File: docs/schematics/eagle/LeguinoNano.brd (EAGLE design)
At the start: 111.4 x 73.7 mm, 32 parts, among them Q1 60V/32A/35m?, Q2 60V/32A/35m?, Q3 60V/32A/35m?, Q4 60V/32A/35m?, Q5 60V/32A/35m?

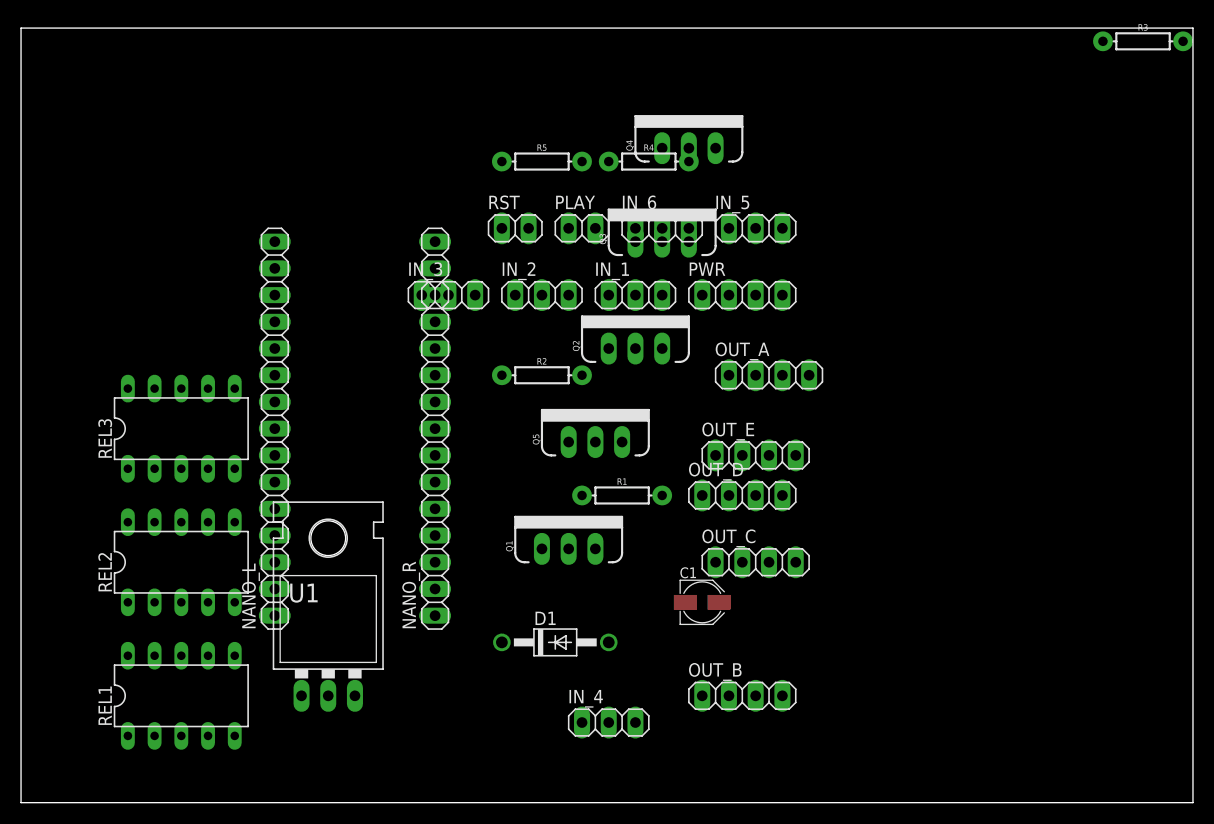
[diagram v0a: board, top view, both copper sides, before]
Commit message: Continued EAGLE schematic and board for Arduino Uno.
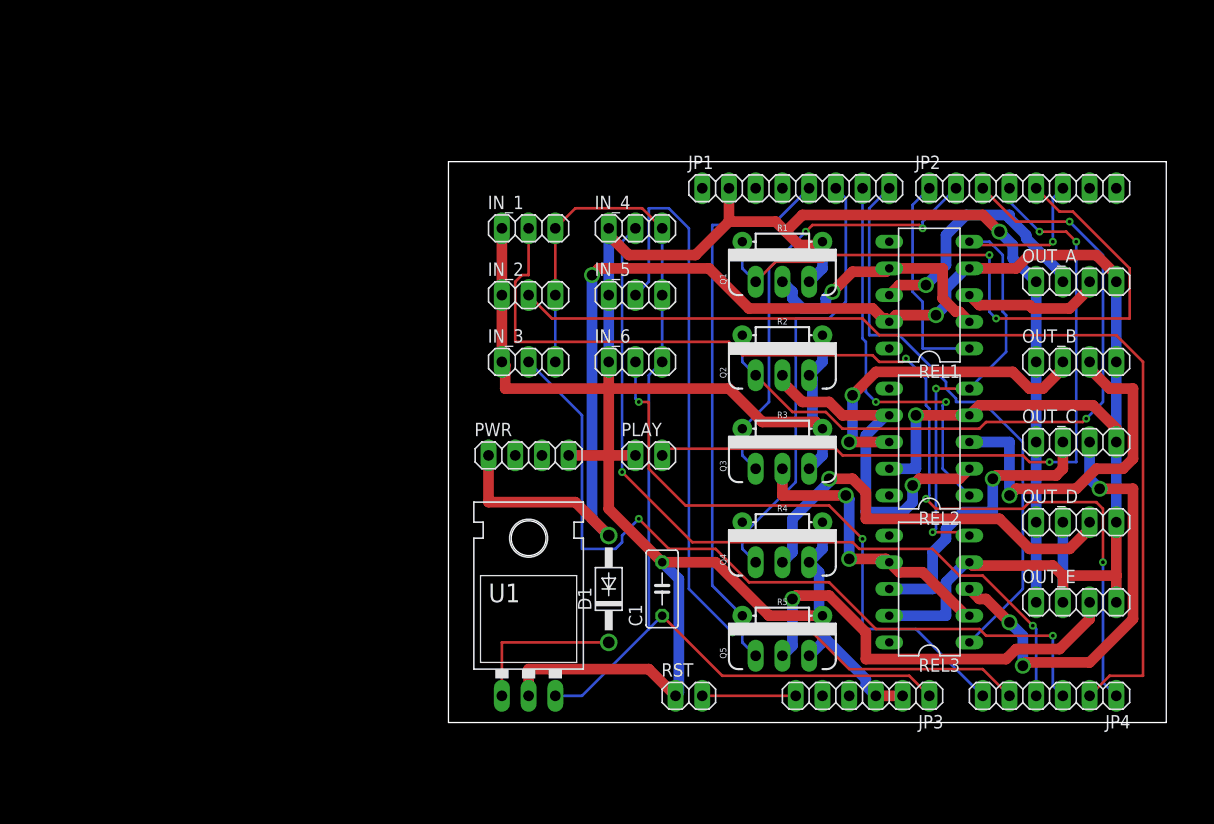
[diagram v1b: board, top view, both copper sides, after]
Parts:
- removed NANO_L, NANO_R: (no value), pinhead:1X15
- added JP1, JP2: (no value), pinhead:1X08
- added JP3, JP4: (no value), pinhead:1X06
- C1: device resistor:PANASONIC_B -> adafruit:C050-030X075
- moved REL1 80.7 mm to (86.4, 48.3), turned to 90 degrees
- moved REL3 72.7 mm to (86.4, 20.3), turned to 90 degrees
- moved REL2 72.0 mm to (86.4, 34.3), turned to 90 degrees
- moved R3 50.3 mm to (72.4, 35.6)
- moved R5 48.9 mm to (72.4, 17.8)
- moved RST 47.4 mm to (63.5, 10.2)
- moved IN_4 47.1 mm to (58.4, 54.6)
- moved OUT_B 44.9 mm to (100.3, 41.9)
- moved Q4 40.4 mm to (72.4, 22.9)
- moved R4 36.6 mm to (72.4, 26.7)
- moved OUT_E 33.5 mm to (100.3, 19.1)
- moved OUT_C 32.6 mm to (100.3, 34.3)
- moved Q1 32.5 mm to (72.4, 49.5)
- moved OUT_D 31.9 mm to (100.3, 26.7)
- moved OUT_A 30.5 mm to (100.3, 49.5)
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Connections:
- removed net N$12: IN_2.3, IN_3.3, IN_4.3, IN_5.3, IN_6.3
- removed net NANO_3V3: NANO_R.14
- removed net NANO_5V: NANO_R.4
- removed net NANO_A0: NANO_R.12
- removed net NANO_A1: NANO_R.11
- removed net NANO_A2: IN_1.2, NANO_R.10
- removed net NANO_A3: IN_2.2, NANO_R.9
- removed net NANO_A4: IN_3.2, NANO_R.8
- removed net NANO_A5: IN_4.2, NANO_R.7
- removed net NANO_A6: IN_5.2, NANO_R.6
- removed net NANO_A7: IN_6.2, NANO_R.5
- removed net NANO_D0: NANO_L.1
- removed net NANO_D1: NANO_L.2
- removed net NANO_D10: NANO_L.13, Q4.1, R4.P$1
- removed net NANO_D11: NANO_L.14, Q5.1, R5.P$1
- removed net NANO_D12: NANO_L.15
- removed net NANO_D13: NANO_R.15
- removed net NANO_D2: NANO_L.5, REL1.5, REL2.5, REL3.5
- removed net NANO_D3: NANO_L.6, Q1.1, R1.P$1
- removed net NANO_D4: NANO_L.7, PLAY.2, Q2.1, R2.P$1
- removed net NANO_D5: NANO_L.8, Q3.1, R3.P$1
- removed net NANO_D6: NANO_L.9
- removed net NANO_D7: NANO_L.10, REL1.1
- removed net NANO_D8: NANO_L.11, REL3.1
- removed net NANO_D9: NANO_L.12, REL2.1
- removed net NANO_GND: NANO_L.4, NANO_R.2
- removed net NANO_REF: NANO_R.13
- removed net NANO_RST: NANO_L.3, NANO_R.3, RST.2
- removed net NANO_VIN: NANO_R.1
- new net UNO_A0: IN_1.2, JP4.1
- new net UNO_A1: IN_2.2, JP4.2
- new net UNO_A2: IN_3.2, JP4.3
- new net UNO_A3: IN_4.2, JP4.4
- new net UNO_A4: IN_5.2, JP4.5
- new net UNO_A5: IN_6.2, JP4.6
- new net UNO_D10: JP1.6, Q4.1, R4.P$1
- new net UNO_D11: JP1.5, Q5.1, R5.P$1
- new net UNO_D2: JP2.6, REL1.5, REL2.5, REL3.5
- new net UNO_D3: JP2.5, Q1.1, R1.P$1
- new net UNO_D4: JP2.4, PLAY.2
- new net UNO_D5: JP2.3, Q2.1, R2.P$1
- new net UNO_D6: JP2.2, Q3.1, R3.P$1
- new net UNO_D7: JP2.1, REL1.1
- new net UNO_D8: JP1.8, REL3.1
- new net UNO_D9: JP1.7, REL2.1
- new net UNO_RST: JP3.6, RST.2
- net GND: now also C1.2, JP1.2, JP3.2, JP3.3; no longer C1.-
- net V+: no longer IN_1.3
- net VCC: now also C1.1, IN_1.3, IN_2.3, IN_3.3, IN_4.3, IN_5.3, IN_6.3, JP3.1; no longer C1.+
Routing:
- net GND: track 0.00 -> 264.6 mm, vias 0 -> 1
- net V+: track 0.00 -> 195.8 mm, vias 0 -> 3
- net VCC: track 0.00 -> 104.9 mm
- net UNO_A0: track 0.00 -> 100.2 mm, vias 0 -> 3
- net UNO_A1: track 0.00 -> 96.8 mm
- net UNO_A4: track 0.00 -> 82.4 mm, vias 0 -> 1
- net UNO_A2: track 0.00 -> 76.9 mm, vias 0 -> 2
- net UNO_A3: track 0.00 -> 75.6 mm, vias 0 -> 2
- net UNO_D4: track 0.00 -> 70.3 mm, vias 0 -> 3
- net UNO_D5: track 0.00 -> 68.5 mm, vias 0 -> 2
- net UNO_D3: track 0.00 -> 63.4 mm, vias 0 -> 2
- net UNO_A5: track 0.00 -> 57.0 mm, vias 0 -> 2
- net UNO_D8: track 0.00 -> 55.3 mm
- net UNO_D11: track 0.00 -> 53.3 mm
- net UNO_D2: track 0.00 -> 52.2 mm, vias 0 -> 3
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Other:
- board size 111.4 x 73.7 mm -> 68.2 x 53.3 mm
